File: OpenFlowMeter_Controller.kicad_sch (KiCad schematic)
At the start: 1 part, among them U2 STM32F103C8Tx

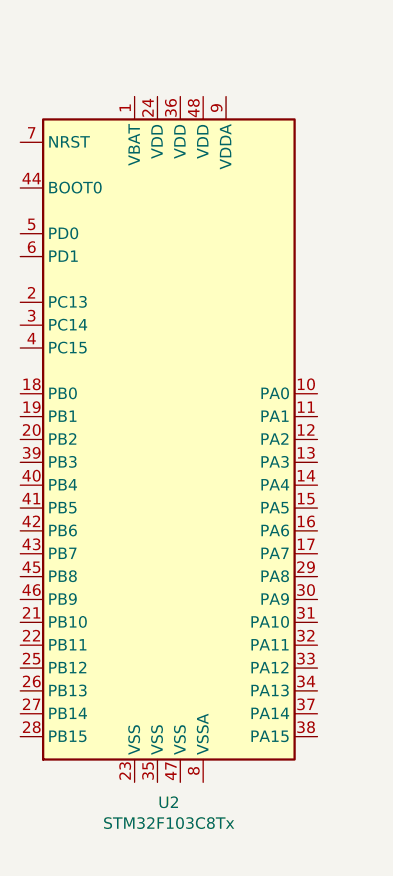
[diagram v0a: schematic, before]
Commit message: intermediate commit
updated schematics and started with controller section

layout proceeded with PWM filter
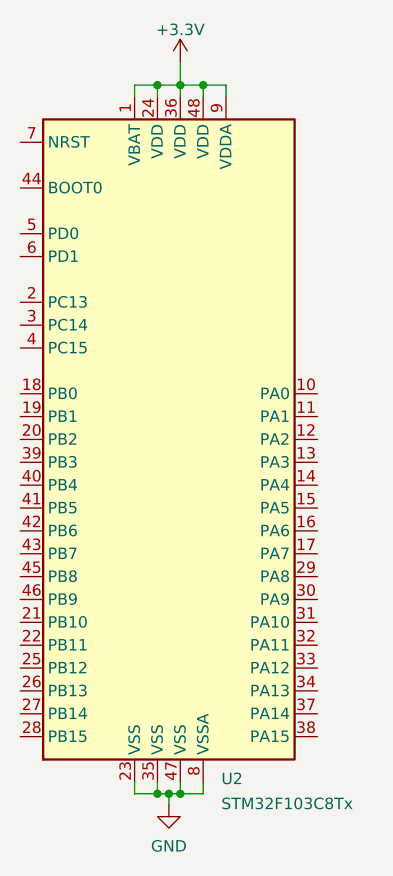
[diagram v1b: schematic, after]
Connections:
- net +3V3: now reaches U2.1 (VBAT)
- net +3V3: now also U2.24 (VDD), U2.36 (VDD), U2.48 (VDD), U2.9 (VDDA)
- net GND: now reaches U2.23 (VSS)
- net GND: now also U2.35 (VSS), U2.47 (VSS), U2.8 (VSSA)
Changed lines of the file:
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@@
     (rev "1")
   )
+  (junction (at 119.38 128.27) (diameter 0) (color 0 0 0 0)
+  )
+  (junction (at 118.11 128.27) (diameter 0) (color 0 0 0 0)
+  )
+  (junction (at 118.11 49.53) (diameter 0) (color 0 0 0 0)
+  )
+  (junction (at 123.19 49.53) (diameter 0) (color 0 0 0 0)
+  )
+  (junction (at 120.65 128.27) (diameter 0) (color 0 0 0 0)
+  )
+  (junction (at 120.65 49.53) (diameter 0) (color 0 0 0 0)
+  )
+  (wire (pts (xy 119.38 128.27) (xy 119.38 129.54))
+    (stroke (width 0) (type default) (color 0 0 0 0))
+  )
+  (wire (pts (xy 115.57 49.53) (xy 115.57 50.8))
+    (stroke (width 0) (type default) (color 0 0 0 0))
+  )
+  (wire (pts (xy 120.65 46.99) (xy 120.65 49.53))
+    (stroke (width 0) (type default) (color 0 0 0 0))
+  )
+  (wire (pts (xy 120.65 127) (xy 120.65 128.27))
+    (stroke (width 0) (type default) (color 0 0 0 0))
+  )
+  (wire (pts (xy 115.57 128.27) (xy 118.11 128.27))
+    (stroke (width 0) (type default) (color 0 0 0 0))
+  )
+  (wire (pts (xy 123.19 127) (xy 123.19 128.27))
+    (stroke (width 0) (type default) (color 0 0 0 0))
+  )
+  (wire (pts (xy 118.11 49.53) (xy 115.57 49.53))
+    (stroke (width 0) (type default) (color 0 0 0 0))
+  )
+  (wire (pts (xy 125.73 50.8) (xy 125.73 49.53))
+    (stroke (width 0) (type default) (color 0 0 0 0))
+  )
+  (wire (pts (xy 120.65 49.53) (xy 120.65 50.8))
+    (stroke (width 0) (type default) (color 0 0 0 0))
+  )
+  (wire (pts (xy 123.19 49.53) (xy 120.65 49.53))
+    (stroke (width 0) (type default) (color 0 0 0 0))
+  )
+  (wire (pts (xy 120.65 128.27) (xy 123.19 128.27))
+    (stroke (width 0) (type default) (color 0 0 0 0))
+  )
+  (wire (pts (xy 119.38 128.27) (xy 120.65 128.27))
+    (stroke (width 0) (type default) (color 0 0 0 0))
+  )
+  (wire (pts (xy 118.11 49.53) (xy 118.11 50.8))
+    (stroke (width 0) (type default) (color 0 0 0 0))
+  )
+  (wire (pts (xy 118.11 127) (xy 118.11 128.27))
+    (stroke (width 0) (type default) (color 0 0 0 0))
+  )
+  (wire (pts (xy 115.57 127) (xy 115.57 128.27))
+    (stroke (width 0) (type default) (color 0 0 0 0))
+  )
+  (wire (pts (xy 123.19 49.53) (xy 123.19 50.8))
+    (stroke (width 0) (type default) (color 0 0 0 0))
+  )
+  (wire (pts (xy 125.73 49.53) (xy 123.19 49.53))
+    (stroke (width 0) (type default) (color 0 0 0 0))
+  )
+  (wire (pts (xy 120.65 49.53) (xy 118.11 49.53))
+    (stroke (width 0) (type default) (color 0 0 0 0))
+  )
+  (wire (pts (xy 118.11 128.27) (xy 119.38 128.27))
+    (stroke (width 0) (type default) (color 0 0 0 0))
+  )
   (symbol (lib_id "MCU_ST_STM32F1:STM32F103C8Tx") (at 120.65 88.9 0) (unit 1)
-    (in_bom yes) (on_board yes)
-    (property "Reference" "U2" (id 0) (at 119.38 129.2606 0))
-    (property "Value" "STM32F103C8Tx" (id 1) (at 119.38 131.572 0))
+    (in_bom yes) (on_board yes) (fields_autoplaced)
+    (property "Reference" "U2" (id 0) (at 125.2094 126.6095 0)
+      (effects (font (size 1.27 1.27)) (justify left))
+    )
+    (property "Value" "STM32F103C8Tx" (id 1) (at 125.2094 129.3846 0)
+      (effects (font (size 1.27 1.27)) (justify left))
+    )
     (property "Footprint" "Package_QFP:LQFP-48_7x7mm_P0.5mm" (id 2) (at 105.41 124.46 0)
       (effects (font (size 1.27 1.27)) (justify right) hide)
@@
     (pin "9")
   )
+  (symbol (lib_id "power:+3.3V") (at 120.65 46.99 0) (unit 1)
+    (in_bom yes) (on_board yes) (fields_autoplaced)
+    (property "Reference" "#PWR0113" (id 0) (at 120.65 50.8 0)
+      (effects (font (size 1.27 1.27)) hide)
+    )
+    (property "Value" "+3.3V" (id 1) (at 120.65 43.3855 0))
+    (property "Footprint" "" (id 2) (at 120.65 46.99 0)
+      (effects (font (size 1.27 1.27)) hide)
+    )
+    (property "Datasheet" "" (id 3) (at 120.65 46.99 0)
+      (effects (font (size 1.27 1.27)) hide)
+    )
+    (pin "1")
+  )
+  (symbol (lib_id "power:GND") (at 119.38 129.54 0) (unit 1)
+    (in_bom yes) (on_board yes) (fields_autoplaced)
+    (property "Reference" "#PWR0114" (id 0) (at 119.38 135.89 0)
+      (effects (font (size 1.27 1.27)) hide)
+    )
+    (property "Value" "GND" (id 1) (at 119.38 134.1025 0))
+    (property "Footprint" "" (id 2) (at 119.38 129.54 0)
+      (effects (font (size 1.27 1.27)) hide)
+    )
+    (property "Datasheet" "" (id 3) (at 119.38 129.54 0)
+      (effects (font (size 1.27 1.27)) hide)
+    )
+    (pin "1")
+  )
 )

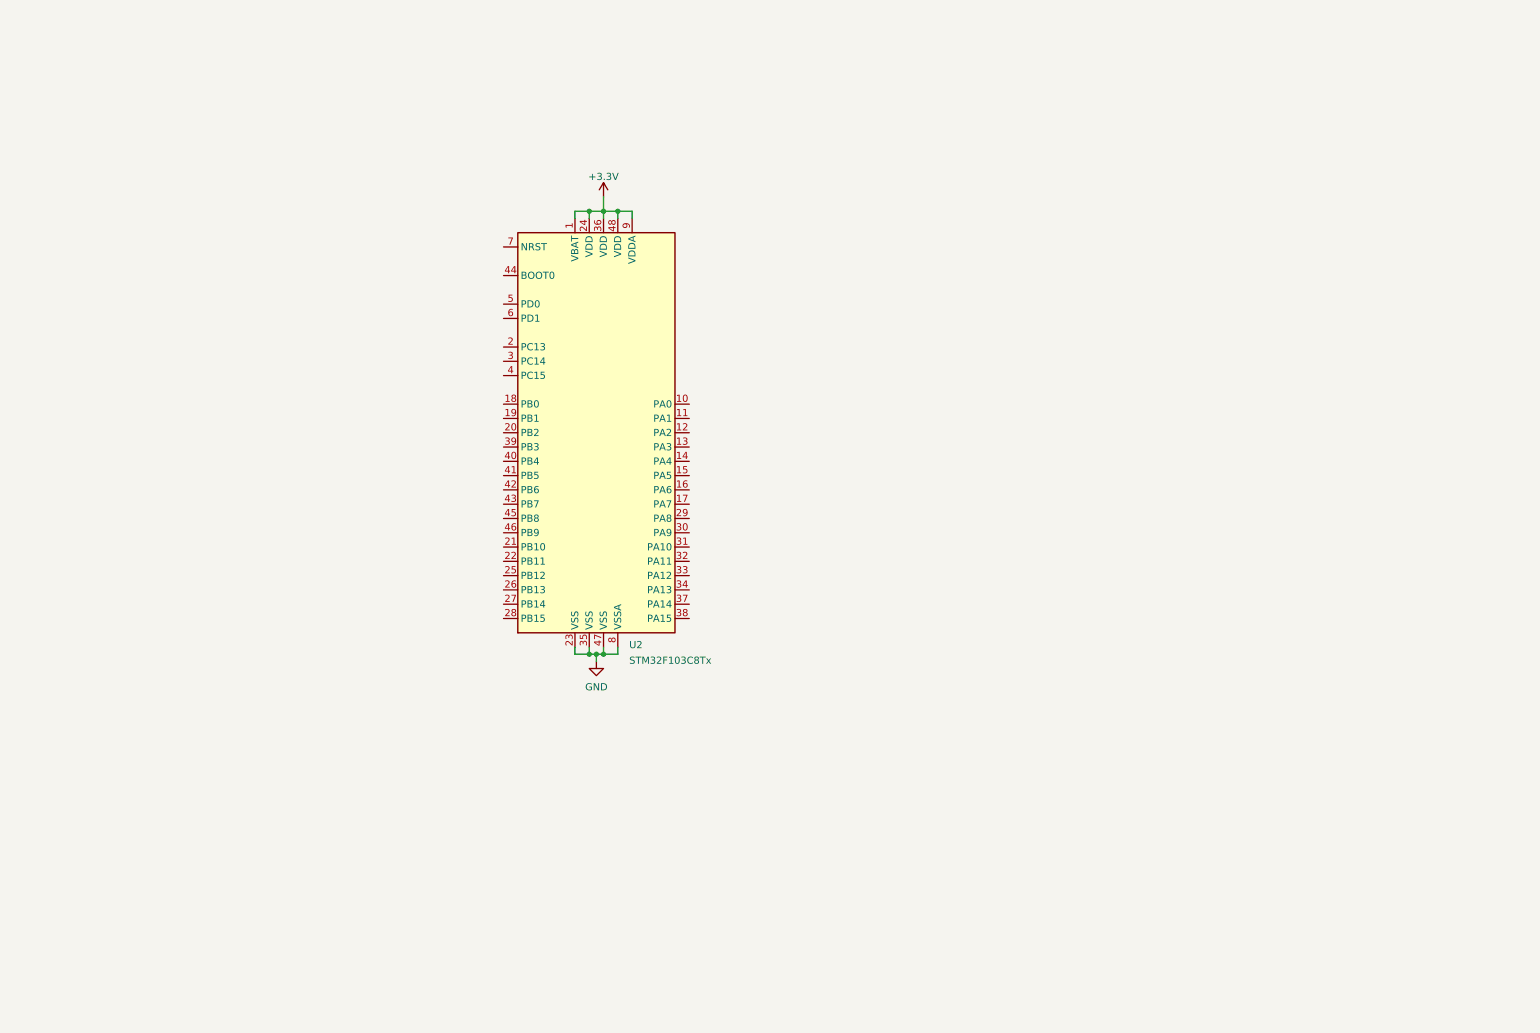
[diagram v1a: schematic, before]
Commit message: Updated controller pin assignment
started thinking again about controller pin assingment.
IOC and SCH matches
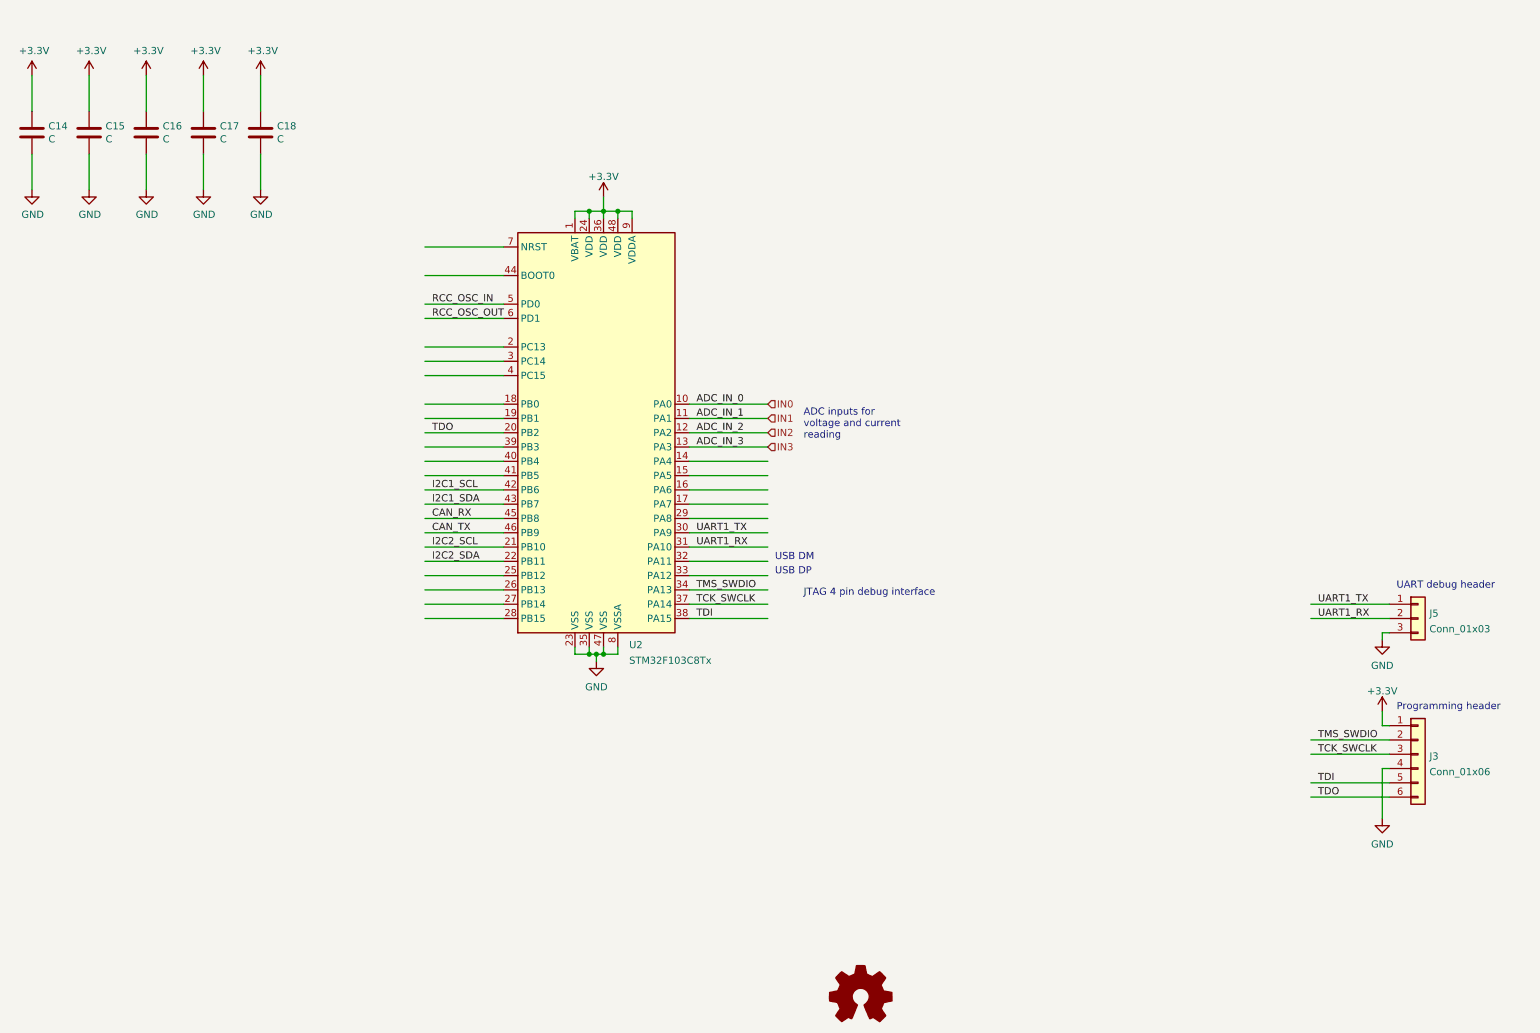
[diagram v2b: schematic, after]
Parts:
- added C14, C15, C16, C17, C18: C, Capacitor_SMD:C_0603_1608Metric_Pad1.08x0.95mm_HandSolder, symbol Device:C
- added J3: Conn_01x06, Connector_PinHeader_2.54mm:PinHeader_1x06_P2.54mm_Vertical, symbol Connector_Generic:Conn_01x06
- added J5: Conn_01x03, Connector_PinHeader_2.54mm:PinHeader_1x03_P2.54mm_Vertical, symbol Connector_Generic:Conn_01x03
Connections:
- net +3V3: now also C14.1, C15.1, C16.1, C17.1, C18.1, J3.1 (Pin_1)
- net GND: now also C14.2, C15.2, C16.2, C17.2, C18.2, J3.4 (Pin_4), J5.3 (Pin_3)
- net IN0: now reaches U2.10 (PA0)
- net IN1: now reaches U2.11 (PA1)
- net IN2: now reaches U2.12 (PA2)
- net IN3: now reaches U2.13 (PA3)
- net TDO: now reaches U2.20 (PB2)
- net TDO: now also J3.6 (Pin_6)
- net I2C2_SCL: now reaches U2.21 (PB10)
- net I2C2_SDA: now reaches U2.22 (PB11)
- net UART1_TX: now reaches U2.30 (PA9)
- net UART1_TX: now also J5.1 (Pin_1)
- net UART1_RX: now reaches U2.31 (PA10)
- net UART1_RX: now also J5.2 (Pin_2)
- net TMS_SWDIO: now reaches U2.34 (PA13)
- net TMS_SWDIO: now also J3.2 (Pin_2)
- net TCK_SWCLK: now reaches U2.37 (PA14)
- net TCK_SWCLK: now also J3.3 (Pin_3)
- net TDI: now reaches U2.38 (PA15)
- net TDI: now also J3.5 (Pin_5)
- net I2C1_SCL: now reaches U2.42 (PB6)
- net I2C1_SDA: now reaches U2.43 (PB7)
- net CAN_RX: now reaches U2.45 (PB8)
- net CAN_TX: now reaches U2.46 (PB9)
- net RCC_OSC_IN: now reaches U2.5 (PD0)
- net RCC_OSC_OUT: now reaches U2.6 (PD1)
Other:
- note added: "ADC inputs for voltage and current reading"
- note added: "JTAG 4 pin debug interface"
- note added: "Programming header"
- note added: "UART debug header"
- note added: "USB DM"
- note added: "USB DP"
